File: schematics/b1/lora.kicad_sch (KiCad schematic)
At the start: 0 parts

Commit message: Added schematic page for the status block.
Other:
- company: (none) -> shawnd.xyz
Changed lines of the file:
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@@
   (title_block
     (title "B1")
-    (date "2024-02-01")
+    (date "2024-02-05")
     (rev "1")
+    (company "shawnd.xyz")
     (comment 2 "scanning as well as radio communications and outputs/displays.")
     (comment 3 "A B1 (Badger One) node is the core hardware unit of the Badger sytem. It handles card")

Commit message: Added schematic page for LoRa.
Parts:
- added C12: 10u, symbol Device:C_Polarized
- added C13: 1u, symbol Device:C
- added C14: 0.1u, symbol Device:C
- added U4: Ai-Thinker-Ra-02, RF_Module:Ai-Thinker-Ra-01-LoRa, symbol RF_Module:Ai-Thinker-Ra-02
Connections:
- new net: C12.1, C13.1, C14.1, U4.3 (VDD)
- new net DIO0: U4.5 (DIO0)
- new net GND: C12.2, C13.2, C14.2, U4.1 (GND), U4.16 (GND), U4.2 (GND), U4.9 (GND)
- new net MISO: U4.13 (MISO)
- new net MOSI: U4.14 (MOSI)
- new net NSS: U4.15 (~{NSS})
- new net RST: U4.4 (~{RESET})
- new net SCK: U4.12 (SCK)
- no-connect marks 0 -> 5
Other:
- title: B1 -> LoRa
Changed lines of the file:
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@@
 (kicad_sch (version 20230121) (generator eeschema)
-  (paper "A4")
+  (paper "A5")
   (title_block
-    (title "B1")
-    (date "2024-02-05")
+    (title "LoRa")
+    (date "2024-02-06")
     (rev "1")
     (company "shawnd.xyz")
-    (comment 2 "scanning as well as radio communications and outputs/displays.")
-    (comment 3 "A B1 (Badger One) node is the core hardware unit of the Badger sytem. It handles card")
+    (comment 3 "wireless communications in case the Wi-Fi connection fails.")
+    (comment 4 "The LoRa block is just an AI Thinker RA-02 LoRa module. This is used for backup")
+  )
+  (junction (at 77.47 46.99) (diameter 0) (color 0 0 0 0)
+  )
+  (junction (at 64.77 46.99) (diameter 0) (color 0 0 0 0)
+  )
+  (junction (at 77.47 36.83) (diameter 0) (color 0 0 0 0)
+  )
+  (junction (at 88.9 36.83) (diameter 0) (color 0 0 0 0)
+  )
+  (no_connect (at 109.22 64.77))
+  (no_connect (at 109.22 72.39))
+  (no_connect (at 109.22 69.85))
+  (no_connect (at 109.22 62.23))
+  (no_connect (at 109.22 67.31))
+  (wire (pts (xy 77.47 46.99) (xy 88.9 46.99))
+    (stroke (width 0) (type default))
+  )
+  (wire (pts (xy 77.47 46.99) (xy 77.47 45.72))
+    (stroke (width 0) (type default))
+  )
+  (wire (pts (xy 88.9 36.83) (xy 88.9 38.1))
+    (stroke (width 0) (type default))
+  )
+  (wire (pts (xy 88.9 46.99) (xy 88.9 45.72))
+    (stroke (width 0) (type default))
+  )
+  (wire (pts (xy 64.77 45.72) (xy 64.77 46.99))
+    (stroke (width 0) (type default))
+  )
+  (wire (pts (xy 88.9 36.83) (xy 77.47 36.83))
+    (stroke (width 0) (type default))
+  )
+  (wire (pts (xy 64.77 38.1) (xy 64.77 36.83))
+    (stroke (width 0) (type default))
+  )
+  (wire (pts (xy 88.9 36.83) (xy 99.06 36.83))
+    (stroke (width 0) (type default))
+  )
+  (wire (pts (xy 99.06 46.99) (xy 99.06 36.83))
+    (stroke (width 0) (type default))
+  )
+  (wire (pts (xy 64.77 48.26) (xy 64.77 46.99))
+    (stroke (width 0) (type default))
+  )
+  (wire (pts (xy 77.47 36.83) (xy 77.47 38.1))
+    (stroke (width 0) (type default))
+  )
+  (wire (pts (xy 64.77 46.99) (xy 77.47 46.99))
+    (stroke (width 0) (type default))
+  )
+  (wire (pts (xy 64.77 36.83) (xy 77.47 36.83))
+    (stroke (width 0) (type default))
+  )
+  (hierarchical_label "RST" (shape input) (at 88.9 72.39 180) (fields_autoplaced)
+    (effects (font (size 1.27 1.27)) (justify right))
+  )
+  (hierarchical_label "MISO" (shape input) (at 88.9 62.23 180) (fields_autoplaced)
+    (effects (font (size 1.27 1.27)) (justify right))
+  )
+  (hierarchical_label "SCK" (shape input) (at 88.9 64.77 180) (fields_autoplaced)
+    (effects (font (size 1.27 1.27)) (justify right))
+  )
+  (hierarchical_label "NSS" (shape input) (at 88.9 67.31 180) (fields_autoplaced)
+    (effects (font (size 1.27 1.27)) (justify right))
+  )
+  (hierarchical_label "DIO0" (shape output) (at 109.22 59.69 0) (fields_autoplaced)
+    (effects (font (size 1.27 1.27)) (justify left))
+  )
+  (hierarchical_label "MOSI" (shape input) (at 88.9 59.69 180) (fields_autoplaced)
+    (effects (font (size 1.27 1.27)) (justify right))
+  )
+  (symbol (lib_id "Device:C") (at 88.9 41.91 0) (unit 1)
+    (in_bom yes) (on_board yes) (dnp no)
+    (property "Reference" "C14" (at 92.71 40.64 0)
+      (effects (font (size 1.27 1.27)) (justify left))
+    )
+    (property "Value" "0.1u" (at 92.71 43.18 0)
+      (effects (font (size 1.27 1.27)) (justify left))
+    )
+    (property "Footprint" "" (at 89.8652 45.72 0)
+      (effects (font (size 1.27 1.27)) hide)
+    )
+    (property "Datasheet" "~" (at 88.9 41.91 0)
+      (effects (font (size 1.27 1.27)) hide)
+    )
+    (pin "2")
+    (pin "1")
+    (instances
+      (project "b1"
+        (path "/d6142fa5-2354-4512-9919-37616259c364/bca829a9-1cbe-4403-a4e4-7724b6c8becd"
+          (reference "C14") (unit 1)
+        )
+      )
+    )
+  )
+  (symbol (lib_id "power:GND") (at 99.06 80.01 0) (unit 1)
+    (in_bom yes) (on_board yes) (dnp no) (fields_autoplaced)
+    (property "Reference" "#PWR022" (at 99.06 86.36 0)
+      (effects (font (size 1.27 1.27)) hide)
+    )
+    (property "Value" "GND" (at 99.06 85.09 0)
+      (effects (font (size 1.27 1.27)))
+    )
+    (property "Footprint" "" (at 99.06 80.01 0)
+      (effects (font (size 1.27 1.27)) hide)
+    )
+    (property "Datasheet" "" (at 99.06 80.01 0)
+      (effects (font (size 1.27 1.27)) hide)
+    )
+    (pin "1")
+    (instances
+      (project "b1"
+        (path "/d6142fa5-2354-4512-9919-37616259c364/bca829a9-1cbe-4403-a4e4-7724b6c8becd"
+          (reference "#PWR022") (unit 1)
+        )
+      )
+    )
+  )
+  (symbol (lib_id "power:GND") (at 64.77 48.26 0) (unit 1)
+    (in_bom yes) (on_board yes) (dnp no) (fields_autoplaced)
+    (property "Reference" "#PWR023" (at 64.77 54.61 0)
+      (effects (font (size 1.27 1.27)) hide)
+    )
+    (property "Value" "GND" (at 64.77 53.34 0)
+      (effects (font (size 1.27 1.27)))
+    )
+    (property "Footprint" "" (at 64.77 48.26 0)
+      (effects (font (size 1.27 1.27)) hide)
+    )
+    (property "Datasheet" "" (at 64.77 48.26 0)
+      (effects (font (size 1.27 1.27)) hide)
+    )
+    (pin "1")
+    (instances
+      (project "b1"
+        (path "/d6142fa5-2354-4512-9919-37616259c364/bca829a9-1cbe-4403-a4e4-7724b6c8becd"
+          (reference "#PWR023") (unit 1)
+        )
+      )
+    )
+  )
+  (symbol (lib_id "Device:C_Polarized") (at 64.77 41.91 0) (unit 1)
+    (in_bom yes) (on_board yes) (dnp no)
+    (property "Reference" "C12" (at 68.58 40.64 0)
+      (effects (font (size 1.27 1.27)) (justify left))
+    )
+    (property "Value" "10u" (at 68.58 43.18 0)
+      (effects (font (size 1.27 1.27)) (justify left))
+    )
+    (property "Footprint" "" (at 65.7352 45.72 0)
+      (effects (font (size 1.27 1.27)) hide)
+    )
+    (property "Datasheet" "~" (at 64.77 41.91 0)
+      (effects (font (size 1.27 1.27)) hide)
+    )
+    (pin "2")
+    (pin "1")
+    (instances
+      (project "b1"
+        (path "/d6142fa5-2354-4512-9919-37616259c364/bca829a9-1cbe-4403-a4e4-7724b6c8becd"
+          (reference "C12") (unit 1)
+        )
+      )
+    )
+  )
+  (symbol (lib_id "RF_Module:Ai-Thinker-Ra-02") (at 99.06 64.77 0) (unit 1)
+    (in_bom yes) (on_board yes) (dnp no) (fields_autoplaced)
+    (property "Reference" "U4" (at 101.2541 46.99 0)
+      (effects (font (size 1.27 1.27)) (justify left))
+    )
+    (property "Value" "Ai-Thinker-Ra-02" (at 101.2541 49.53 0)
+      (effects (font (size 1.27 1.27)) (justify left))
+    )
+    (property "Footprint" "RF_Module:Ai-Thinker-Ra-01-LoRa" (at 124.46 74.93 0)
+      (effects (font (size 1.27 1.27)) hide)
+    )
+    (property "Datasheet" "http://wiki.ai-thinker.com/_media/lora/docs/c048ps01a1_ra-02_product_specification_v1.1.pdf" (at 101.6 45.72 0)
+      (effects (font (size 1.27 1.27)) hide)
+    )
+    (pin "5")
+    (pin "1")
+    (pin "6")
+    (pin "7")
+    (pin "4")
+    (pin "3")
+    (pin "2")
+    (pin "13")
+    (pin "9")
+    (pin "11")
+    (pin "15")
+    (pin "14")
+    (pin "12")
+    (pin "10")
+    (pin "16")
+    (pin "8")
+    (instances
+      (project "b1"
+        (path "/d6142fa5-2354-4512-9919-37616259c364/bca829a9-1cbe-4403-a4e4-7724b6c8becd"
+          (reference "U4") (unit 1)
+        )
+      )
+    )
+  )
+  (symbol (lib_id "Device:C") (at 77.47 41.91 0) (unit 1)
+    (in_bom yes) (on_board yes) (dnp no) (fields_autoplaced)
+    (property "Reference" "C13" (at 81.28 40.64 0)
+      (effects (font (size 1.27 1.27)) (justify left))
+    )
+    (property "Value" "1u" (at 81.28 43.18 0)
+      (effects (font (size 1.27 1.27)) (justify left))
+    )
+    (property "Footprint" "" (at 78.4352 45.72 0)
+      (effects (font (size 1.27 1.27)) hide)
+    )
+    (property "Datasheet" "~" (at 77.47 41.91 0)
+      (effects (font (size 1.27 1.27)) hide)
+    )
+    (pin "2")
+    (pin "1")
+    (instances
+      (project "b1"
+        (path "/d6142fa5-2354-4512-9919-37616259c364/bca829a9-1cbe-4403-a4e4-7724b6c8becd"
+          (reference "C13") (unit 1)
+        )
+      )
+    )
   )
 )

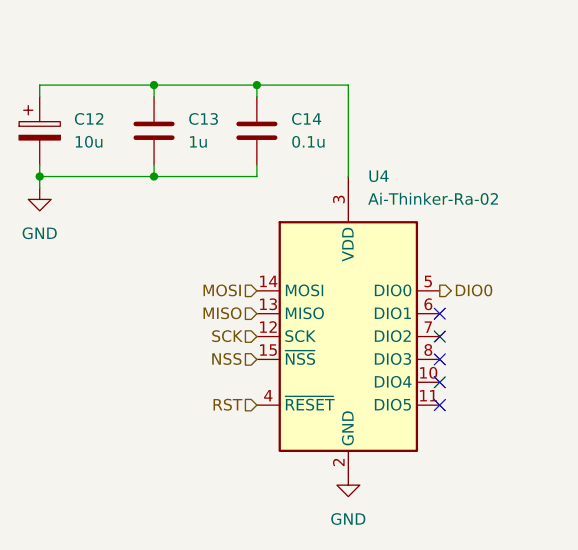
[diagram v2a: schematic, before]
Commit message: Added schematic page for e-paper block.
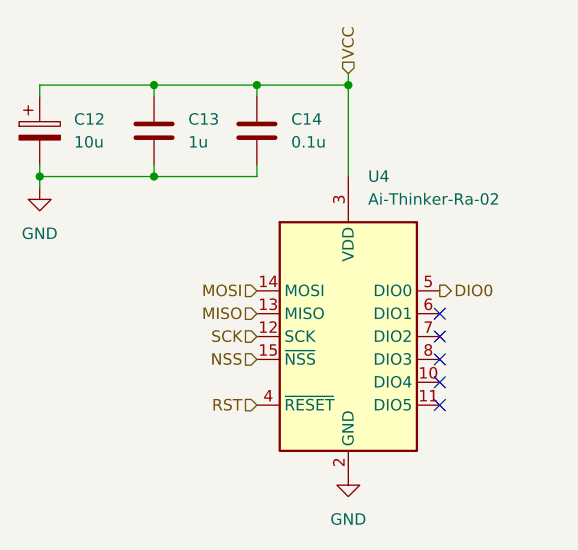
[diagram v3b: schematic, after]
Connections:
- net VCC: now reaches C12.1, C13.1, C14.1, U4.3 (VDD)
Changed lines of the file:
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@@
   (junction (at 77.47 46.99) (diameter 0) (color 0 0 0 0)
+  )
+  (junction (at 99.06 36.83) (diameter 0) (color 0 0 0 0)
   )
   (junction (at 64.77 46.99) (diameter 0) (color 0 0 0 0)
@@
     (stroke (width 0) (type default))
   )
+  (wire (pts (xy 99.06 35.56) (xy 99.06 36.83))
+    (stroke (width 0) (type default))
+  )
   (wire (pts (xy 77.47 36.83) (xy 77.47 38.1))
     (stroke (width 0) (type default))
@@
     (effects (font (size 1.27 1.27)) (justify right))
   )
+  (hierarchical_label "VCC" (shape input) (at 99.06 35.56 90) (fields_autoplaced)
+    (effects (font (size 1.27 1.27)) (justify left))
+  )
   (hierarchical_label "NSS" (shape input) (at 88.9 67.31 180) (fields_autoplaced)

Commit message: Updated labels.
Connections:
- net NSS renamed ~{NSS}
- net RST renamed ~{RESET}
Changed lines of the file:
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@@
     (stroke (width 0) (type default))
   )
-  (hierarchical_label "RST" (shape input) (at 88.9 72.39 180) (fields_autoplaced)
+  (hierarchical_label "~{RESET}" (shape input) (at 88.9 72.39 180) (fields_autoplaced)
     (effects (font (size 1.27 1.27)) (justify right))
   )
@@
     (effects (font (size 1.27 1.27)) (justify left))
   )
-  (hierarchical_label "NSS" (shape input) (at 88.9 67.31 180) (fields_autoplaced)
+  (hierarchical_label "~{NSS}" (shape input) (at 88.9 67.31 180) (fields_autoplaced)
     (effects (font (size 1.27 1.27)) (justify right))
   )

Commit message: General schematic updates.
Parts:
- renumbered U4 to U1
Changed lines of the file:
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@@
     (effects (font (size 1.27 1.27)) (justify right))
   )
-  (hierarchical_label "MISO" (shape input) (at 88.9 62.23 180) (fields_autoplaced)
-    (effects (font (size 1.27 1.27)) (justify right))
+  (hierarchical_label "MISO" (shape output) (at 109.22 57.15 0) (fields_autoplaced)
+    (effects (font (size 1.27 1.27)) (justify left))
   )
   (hierarchical_label "SCK" (shape input) (at 88.9 64.77 180) (fields_autoplaced)
@@
   (symbol (lib_id "power:GND") (at 99.06 80.01 0) (unit 1)
     (in_bom yes) (on_board yes) (dnp no) (fields_autoplaced)
-    (property "Reference" "#PWR022" (at 99.06 86.36 0)
+    (property "Reference" "#PWR02" (at 99.06 86.36 0)
       (effects (font (size 1.27 1.27)) hide)
     )
@@
       (project "b1"
         (path "/d6142fa5-2354-4512-9919-37616259c364/bca829a9-1cbe-4403-a4e4-7724b6c8becd"
-          (reference "#PWR022") (unit 1)
+          (reference "#PWR02") (unit 1)
         )
       )
@@
   (symbol (lib_id "power:GND") (at 64.77 48.26 0) (unit 1)
     (in_bom yes) (on_board yes) (dnp no) (fields_autoplaced)
-    (property "Reference" "#PWR023" (at 64.77 54.61 0)
+    (property "Reference" "#PWR01" (at 64.77 54.61 0)
       (effects (font (size 1.27 1.27)) hide)
     )
@@
       (project "b1"
         (path "/d6142fa5-2354-4512-9919-37616259c364/bca829a9-1cbe-4403-a4e4-7724b6c8becd"
-          (reference "#PWR023") (unit 1)
+          (reference "#PWR01") (unit 1)
         )
       )
@@
   (symbol (lib_id "RF_Module:Ai-Thinker-Ra-02") (at 99.06 64.77 0) (unit 1)
     (in_bom yes) (on_board yes) (dnp no) (fields_autoplaced)
-    (property "Reference" "U4" (at 101.2541 46.99 0)
+    (property "Reference" "U1" (at 101.2541 46.99 0)
       (effects (font (size 1.27 1.27)) (justify left))
     )
@@
       (project "b1"
         (path "/d6142fa5-2354-4512-9919-37616259c364/bca829a9-1cbe-4403-a4e4-7724b6c8becd"
-          (reference "U4") (unit 1)
+          (reference "U1") (unit 1)
         )
       )
